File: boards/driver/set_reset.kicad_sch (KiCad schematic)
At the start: 22 parts, among them Q62 MMBT2222, Q63 MMBT2907, Q64 MMBT2222, Q65 MMBT2222

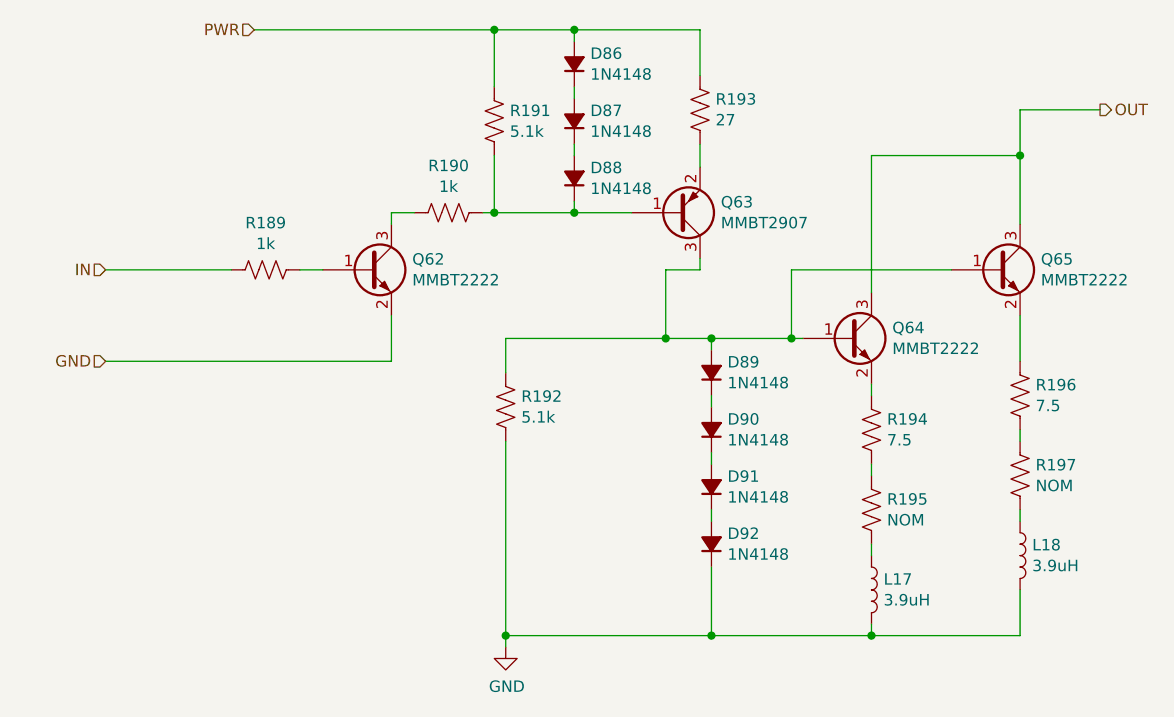
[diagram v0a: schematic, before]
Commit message: Driver: Added a 5V->3.3V LDO to replace the reversed cmod header, added jumpers for the 200R parallel returns, and renamed subcircuit ports to avoid unexpected ground connections.
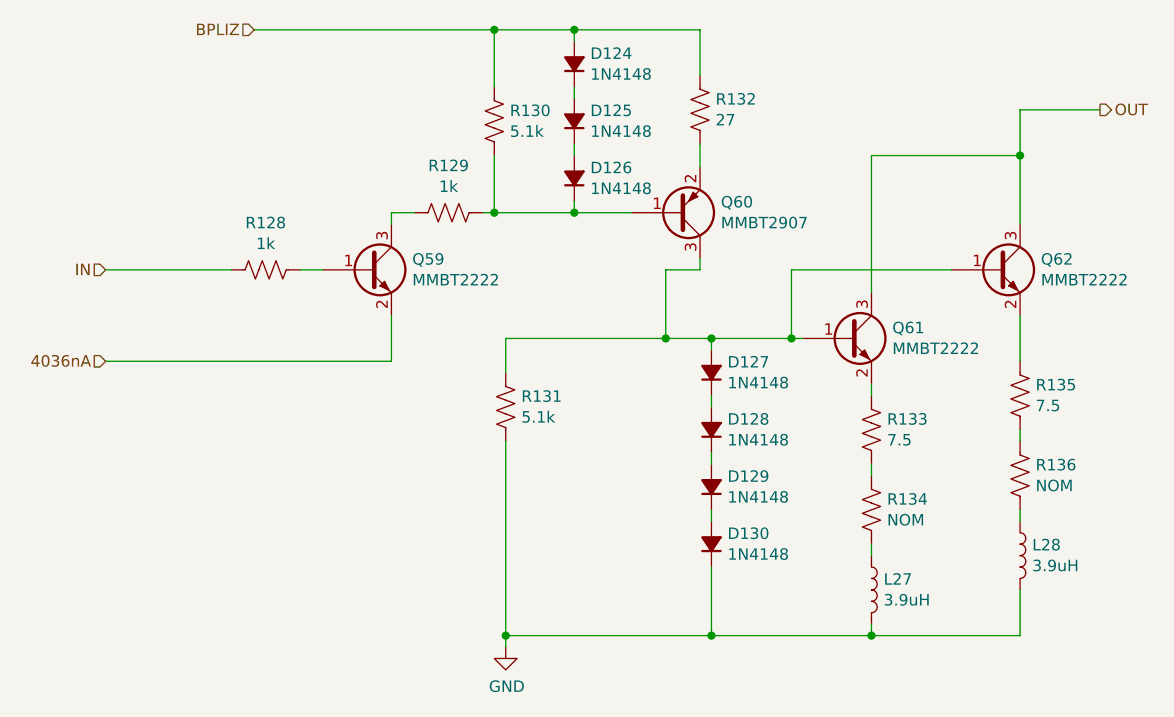
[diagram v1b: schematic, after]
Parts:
- renumbered D86 to D124, D87 to D125, D88 to D126, D89 to D127, D90 to D128, D91 to D129, D92 to D130, L17 to L27, L18 to L28, Q62 to Q59, Q63 to Q60, Q64 to Q61, Q65 to Q62, R189 to R128, R190 to R129, R191 to R130, R192 to R131, R193 to R132, R194 to R133, R195 to R134, R196 to R135, R197 to R136
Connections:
- net GND: no longer Q59.2 (E)
- net PWR renamed BPLIZ
- new net 4036nA: Q59.2 (E)
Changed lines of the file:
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@@
     (stroke (width 0) (type default) (color 0 0 0 0))
   )
-  (hierarchical_label "PWR" (shape input) (at 100.33 63.5 180)
+  (hierarchical_label "BPLIZ" (shape input) (at 100.33 63.5 180)
     (effects (font (size 1.27 1.27)) (justify right))
   )
@@
     (effects (font (size 1.27 1.27)) (justify left))
   )
-  (hierarchical_label "GND" (shape input) (at 83.82 100.33 180)
+  (hierarchical_label "4036nA" (shape input) (at 83.82 100.33 180)
     (effects (font (size 1.27 1.27)) (justify right))
   )
@@
   (symbol (lib_id "Device:R_US") (at 101.6 90.17 270)
     (in_bom yes) (on_board yes)
-    (property "Reference" "R189" (id 0) (at 101.6 84.963 90))
+    (property "Reference" "R128" (id 0) (at 101.6 84.963 90))
     (property "Value" "1k" (id 1) (at 101.6 87.2744 90))
     (property "Footprint" "Resistor_SMD:R_0603_1608Metric" (id 2) (at 101.346 91.186 90)
@@
   (symbol (lib_id "Device:Q_NPN_BEC") (at 113.03 90.17 0)
     (in_bom yes) (on_board yes)
-    (property "Reference" "Q62" (id 0) (at 117.8814 89.0016 0)
+    (property "Reference" "Q59" (id 0) (at 117.8814 89.0016 0)
       (effects (font (size 1.27 1.27)) (justify left))
     )
@@
   (symbol (lib_id "Device:R_US") (at 121.92 83.82 270)
     (in_bom yes) (on_board yes)
-    (property "Reference" "R190" (id 0) (at 121.92 78.613 90))
+    (property "Reference" "R129" (id 0) (at 121.92 78.613 90))
     (property "Value" "1k" (id 1) (at 121.92 80.9244 90))
     (property "Footprint" "Resistor_SMD:R_0603_1608Metric" (id 2) (at 121.666 84.836 90)
@@
   (symbol (lib_id "Device:R_US") (at 127 73.66 0)
     (in_bom yes) (on_board yes)
-    (property "Reference" "R191" (id 0) (at 128.7272 72.4916 0)
+    (property "Reference" "R130" (id 0) (at 128.7272 72.4916 0)
       (effects (font (size 1.27 1.27)) (justify left))
     )
@@
   (symbol (lib_id "Device:D_Small_Filled") (at 135.89 80.01 90)
     (in_bom yes) (on_board yes)
-    (property "Reference" "D88" (id 0) (at 137.668 78.8416 90)
+    (property "Reference" "D126" (id 0) (at 137.668 78.8416 90)
       (effects (font (size 1.27 1.27)) (justify right))
     )
@@
   (symbol (lib_id "Device:D_Small_Filled") (at 135.89 73.66 90)
     (in_bom yes) (on_board yes)
-    (property "Reference" "D87" (id 0) (at 137.668 72.4916 90)
+    (property "Reference" "D125" (id 0) (at 137.668 72.4916 90)
       (effects (font (size 1.27 1.27)) (justify right))
     )
@@
   (symbol (lib_id "Device:D_Small_Filled") (at 135.89 67.31 90)
     (in_bom yes) (on_board yes)
-    (property "Reference" "D86" (id 0) (at 137.668 66.1416 90)
+    (property "Reference" "D124" (id 0) (at 137.668 66.1416 90)
       (effects (font (size 1.27 1.27)) (justify right))
     )
@@
   (symbol (lib_id "Device:Q_PNP_BEC") (at 147.32 83.82 0) (mirror x)
     (in_bom yes) (on_board yes)
-    (property "Reference" "Q63" (id 0) (at 152.1714 82.6516 0)
+    (property "Reference" "Q60" (id 0) (at 152.1714 82.6516 0)
       (effects (font (size 1.27 1.27)) (justify left))
     )
@@
   (symbol (lib_id "Device:R_US") (at 149.86 72.39 0)
     (in_bom yes) (on_board yes)
-    (property "Reference" "R193" (id 0) (at 151.5872 71.2216 0)
+    (property "Reference" "R132" (id 0) (at 151.5872 71.2216 0)
       (effects (font (size 1.27 1.27)) (justify left))
     )
@@
   (symbol (lib_id "Device:D_Small_Filled") (at 151.13 114.3 90)
     (in_bom yes) (on_board yes)
-    (property "Reference" "D91" (id 0) (at 152.908 113.1316 90)
+    (property "Reference" "D129" (id 0) (at 152.908 113.1316 90)
       (effects (font (size 1.27 1.27)) (justify right))
     )
@@
   (symbol (lib_id "Device:D_Small_Filled") (at 151.13 107.95 90)
     (in_bom yes) (on_board yes)
-    (property "Reference" "D90" (id 0) (at 152.908 106.7816 90)
+    (property "Reference" "D128" (id 0) (at 152.908 106.7816 90)
       (effects (font (size 1.27 1.27)) (justify right))
     )
@@
   (symbol (lib_id "Device:D_Small_Filled") (at 151.13 101.6 90)
     (in_bom yes) (on_board yes)
-    (property "Reference" "D89" (id 0) (at 152.908 100.4316 90)
+    (property "Reference" "D127" (id 0) (at 152.908 100.4316 90)
       (effects (font (size 1.27 1.27)) (justify right))
     )
@@
   (symbol (lib_id "Device:D_Small_Filled") (at 151.13 120.65 90)
     (in_bom yes) (on_board yes)
-    (property "Reference" "D92" (id 0) (at 152.908 119.4816 90)
+    (property "Reference" "D130" (id 0) (at 152.908 119.4816 90)
       (effects (font (size 1.27 1.27)) (justify right))
     )
@@
   (symbol (lib_id "Device:R_US") (at 128.27 105.41 0)
     (in_bom yes) (on_board yes)
-    (property "Reference" "R192" (id 0) (at 129.9972 104.2416 0)
+    (property "Reference" "R131" (id 0) (at 129.9972 104.2416 0)
       (effects (font (size 1.27 1.27)) (justify left))
     )
@@
   (symbol (lib_id "power:GND") (at 128.27 132.08 0)
     (in_bom yes) (on_board yes)
-    (property "Reference" "#PWR099" (id 0) (at 128.27 138.43 0)
+    (property "Reference" "#PWR028" (id 0) (at 128.27 138.43 0)
       (effects (font (size 1.27 1.27)) hide)
     )
@@
   (symbol (lib_id "Device:Q_NPN_BEC") (at 166.37 97.79 0)
     (in_bom yes) (on_board yes)
-    (property "Reference" "Q64" (id 0) (at 171.2214 96.6216 0)
+    (property "Reference" "Q61" (id 0) (at 171.2214 96.6216 0)
       (effects (font (size 1.27 1.27)) (justify left))
     )
@@
   (symbol (lib_id "Device:Q_NPN_BEC") (at 182.88 90.17 0)
     (in_bom yes) (on_board yes)
-    (property "Reference" "Q65" (id 0) (at 187.7314 89.0016 0)
+    (property "Reference" "Q62" (id 0) (at 187.7314 89.0016 0)
       (effects (font (size 1.27 1.27)) (justify left))
     )
@@
   (symbol (lib_id "Device:R_US") (at 168.91 107.95 0)
     (in_bom yes) (on_board yes)
-    (property "Reference" "R194" (id 0) (at 170.6372 106.7816 0)
+    (property "Reference" "R133" (id 0) (at 170.6372 106.7816 0)
       (effects (font (size 1.27 1.27)) (justify left))
     )
@@
   (symbol (lib_id "Device:L") (at 168.91 125.73 0)
     (in_bom yes) (on_board yes)
-    (property "Reference" "L17" (id 0) (at 170.2562 124.5616 0)
+    (property "Reference" "L27" (id 0) (at 170.2562 124.5616 0)
       (effects (font (size 1.27 1.27)) (justify left))
     )
@@
   (symbol (lib_id "Device:R_US") (at 185.42 104.14 0)
     (in_bom yes) (on_board yes)
-    (property "Reference" "R196" (id 0) (at 187.1472 102.9716 0)
+    (property "Reference" "R135" (id 0) (at 187.1472 102.9716 0)
       (effects (font (size 1.27 1.27)) (justify left))
     )
@@
   (symbol (lib_id "Device:L") (at 185.42 121.92 0)
     (in_bom yes) (on_board yes)
-    (property "Reference" "L18" (id 0) (at 186.7662 120.7516 0)
+    (property "Reference" "L28" (id 0) (at 186.7662 120.7516 0)
       (effects (font (size 1.27 1.27)) (justify left))
     )
@@
   (symbol (lib_id "Device:R_US") (at 168.91 116.84 0)
     (in_bom yes) (on_board yes)
-    (property "Reference" "R195" (id 0) (at 170.6372 115.6716 0)
+    (property "Reference" "R134" (id 0) (at 170.6372 115.6716 0)
       (effects (font (size 1.27 1.27)) (justify left))
     )
@@
   (symbol (lib_id "Device:R_US") (at 185.42 113.03 0)
     (in_bom yes) (on_board yes)
-    (property "Reference" "R197" (id 0) (at 187.1472 111.8616 0)
-      (effects (font (size 1.27 1.27)) (justify left))
-    )
+    (property "Reference" "R136" (id 0) (at 187.1472 111.8616 0)
+      (effects (font (size 1.27 1.27)) (justify left))
+    )

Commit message: Driver: incorporated most changes from the test board, and began layout
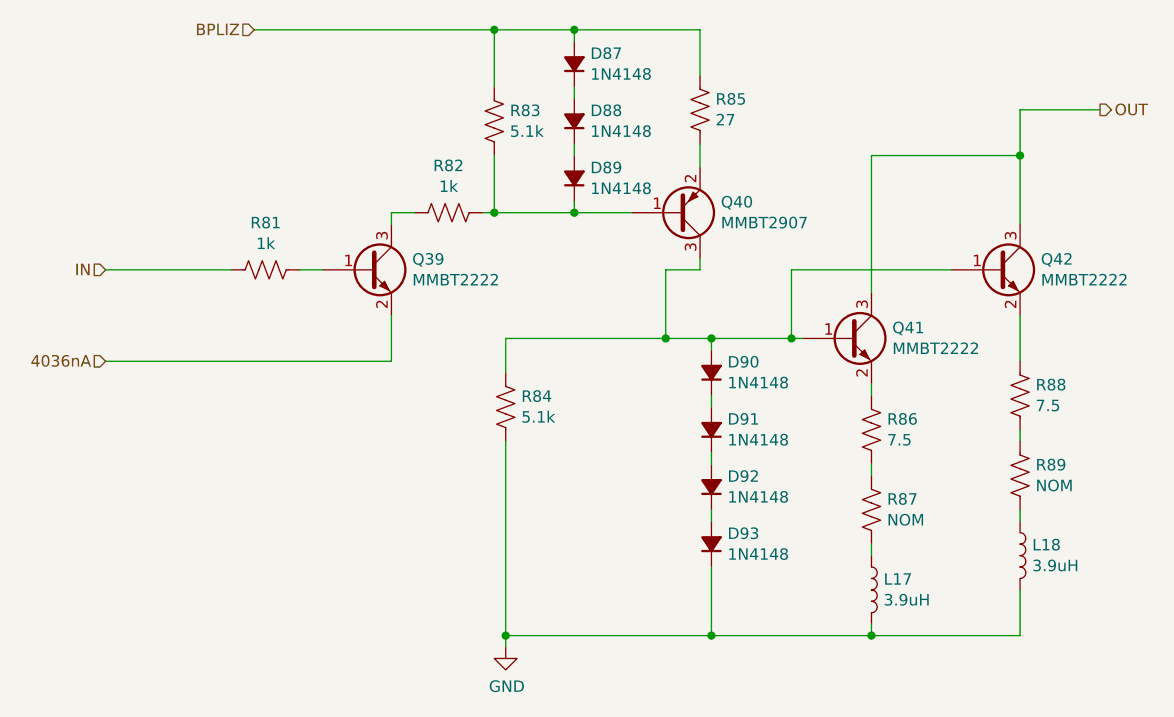
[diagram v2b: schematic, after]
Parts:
- D87: renamed from D124; footprint Diode_SMD:D_SOD-323 -> lachesis:D_SOD-323
- D88: renamed from D125; footprint Diode_SMD:D_SOD-323 -> lachesis:D_SOD-323
- D89: renamed from D126; footprint Diode_SMD:D_SOD-323 -> lachesis:D_SOD-323
- D90: renamed from D127; footprint Diode_SMD:D_SOD-323 -> lachesis:D_SOD-323
- D91: renamed from D128; footprint Diode_SMD:D_SOD-323 -> lachesis:D_SOD-323
- D92: renamed from D129; footprint Diode_SMD:D_SOD-323 -> lachesis:D_SOD-323
- D93: renamed from D130; footprint Diode_SMD:D_SOD-323 -> lachesis:D_SOD-323
- L17: renamed from L27; footprint Inductor_SMD:L_1812_4532Metric -> lachesis:API_Delevan_1812R
- L18: renamed from L28; footprint Inductor_SMD:L_1812_4532Metric -> lachesis:API_Delevan_1812R
- renumbered Q59 to Q39, Q60 to Q40, Q61 to Q41, Q62 to Q42, R128 to R81, R129 to R82, R130 to R83, R131 to R84, R132 to R85, R133 to R86, R134 to R87, R135 to R88, R136 to R89

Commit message: Driver: minor schematic cleanup and populated all of the BOM except for resistors
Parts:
- D87, D88, D89, D90, D91, D92, D93: MPN (none) -> 1N4148WS; Manufacturer (none) -> SMC Diode Solutions; Package (none) -> SOD-323; Rating (none) -> 300mA
- L17, L18: MPN (none) -> 1812R-392J; Manufacturer (none) -> API Delevan Inc; Package (none) -> 1812
- Q39, Q41, Q42: MPN (none) -> MMBT2222ALT1HTSA1; Manufacturer (none) -> Infineon Technologies; Package (none) -> SOT-23-3
- Q40: MPN (none) -> MMBT2907ALT1HTSA1; Manufacturer (none) -> Infineon Technologies; Package (none) -> SOT-23-3
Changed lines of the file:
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@@
+      (effects (font (size 1.27 1.27)) hide)
+    )
+    (property "MPN" "MMBT2222ALT1HTSA1" (id 6) (at 113.03 90.17 0)
+      (effects (font (size 1.27 1.27)) hide)
+    )
+    (property "Manufacturer" "Infineon Technologies" (id 7) (at 113.03 90.17 0)
+      (effects (font (size 1.27 1.27)) hide)
+    )
+    (property "Description" "TRANS NPN 40V 0.6A SOT-23" (id 8) (at 113.03 90.17 0)
+      (effects (font (size 1.27 1.27)) hide)
+    )
+    (property "Package" "SOT-23-3" (id 9) (at 113.03 90.17 0)
       (effects (font (size 1.27 1.27)) hide)
     )
@@
       (effects (font (size 1.27 1.27)) hide)
     )
+    (property "MPN" "1N4148WS" (id 6) (at 135.89 80.01 0)
+      (effects (font (size 1.27 1.27)) hide)
+    )
+    (property "Manufacturer" "SMC Diode Solutions" (id 7) (at 135.89 80.01 0)
+      (effects (font (size 1.27 1.27)) hide)
+    )
+    (property "Description" "DIODE GEN PURP 75V 300MA SOD323" (id 8) (at 135.89 80.01 0)
+      (effects (font (size 1.27 1.27)) hide)
+    )
+    (property "Package" "SOD-323" (id 9) (at 135.89 80.01 0)
+      (effects (font (size 1.27 1.27)) hide)
+    )
+    (property "Rating" "300mA" (id 10) (at 135.89 80.01 0)
+      (effects (font (size 1.27 1.27)) hide)
+    )
     (pin "1")
     (pin "2")
@@
       (effects (font (size 1.27 1.27)) hide)
     )
+    (property "MPN" "1N4148WS" (id 6) (at 135.89 73.66 0)
+      (effects (font (size 1.27 1.27)) hide)
+    )
+    (property "Manufacturer" "SMC Diode Solutions" (id 7) (at 135.89 73.66 0)
+      (effects (font (size 1.27 1.27)) hide)
+    )
+    (property "Description" "DIODE GEN PURP 75V 300MA SOD323" (id 8) (at 135.89 73.66 0)
+      (effects (font (size 1.27 1.27)) hide)
+    )
+    (property "Package" "SOD-323" (id 9) (at 135.89 73.66 0)
+      (effects (font (size 1.27 1.27)) hide)
+    )
+    (property "Rating" "300mA" (id 10) (at 135.89 73.66 0)
+      (effects (font (size 1.27 1.27)) hide)
+    )
     (pin "1")
     (pin "2")
@@
       (effects (font (size 1.27 1.27)) hide)
     )
+    (property "MPN" "1N4148WS" (id 6) (at 135.89 67.31 0)
+      (effects (font (size 1.27 1.27)) hide)
+    )
+    (property "Manufacturer" "SMC Diode Solutions" (id 7) (at 135.89 67.31 0)
+      (effects (font (size 1.27 1.27)) hide)
+    )
+    (property "Description" "DIODE GEN PURP 75V 300MA SOD323" (id 8) (at 135.89 67.31 0)
+      (effects (font (size 1.27 1.27)) hide)
+    )
+    (property "Package" "SOD-323" (id 9) (at 135.89 67.31 0)
+      (effects (font (size 1.27 1.27)) hide)
+    )
+    (property "Rating" "300mA" (id 10) (at 135.89 67.31 0)
+      (effects (font (size 1.27 1.27)) hide)
+    )
     (pin "1")
     (pin "2")
@@
       (effects (font (size 1.27 1.27)) hide)
     )
+    (property "MPN" "MMBT2907ALT1HTSA1" (id 6) (at 147.32 83.82 0)
+      (effects (font (size 1.27 1.27)) hide)
+    )
+    (property "Manufacturer" "Infineon Technologies" (id 7) (at 147.32 83.82 0)
+      (effects (font (size 1.27 1.27)) hide)
+    )
+    (property "Description" "TRANS PNP 60V 0.6A SOT23" (id 8) (at 147.32 83.82 0)
+      (effects (font (size 1.27 1.27)) hide)
+    )
+    (property "Package" "SOT-23-3" (id 9) (at 147.32 83.82 0)
+      (effects (font (size 1.27 1.27)) hide)
+    )
     (pin "1")
     (pin "2")
@@
       (effects (font (size 1.27 1.27)) hide)
     )
+    (property "MPN" "1N4148WS" (id 6) (at 151.13 114.3 0)
+      (effects (font (size 1.27 1.27)) hide)
+    )
+    (property "Manufacturer" "SMC Diode Solutions" (id 7) (at 151.13 114.3 0)
+      (effects (font (size 1.27 1.27)) hide)
+    )
+    (property "Description" "DIODE GEN PURP 75V 300MA SOD323" (id 8) (at 151.13 114.3 0)
+      (effects (font (size 1.27 1.27)) hide)
+    )
+    (property "Package" "SOD-323" (id 9) (at 151.13 114.3 0)
+      (effects (font (size 1.27 1.27)) hide)
+    )
+    (property "Rating" "300mA" (id 10) (at 151.13 114.3 0)
+      (effects (font (size 1.27 1.27)) hide)
+    )
     (pin "1")
     (pin "2")
@@
       (effects (font (size 1.27 1.27)) hide)
     )
+    (property "MPN" "1N4148WS" (id 6) (at 151.13 107.95 0)
+      (effects (font (size 1.27 1.27)) hide)
+    )
+    (property "Manufacturer" "SMC Diode Solutions" (id 7) (at 151.13 107.95 0)
+      (effects (font (size 1.27 1.27)) hide)
+    )
+    (property "Description" "DIODE GEN PURP 75V 300MA SOD323" (id 8) (at 151.13 107.95 0)
+      (effects (font (size 1.27 1.27)) hide)
+    )
+    (property "Package" "SOD-323" (id 9) (at 151.13 107.95 0)
+      (effects (font (size 1.27 1.27)) hide)
+    )
+    (property "Rating" "300mA" (id 10) (at 151.13 107.95 0)
+      (effects (font (size 1.27 1.27)) hide)
+    )
     (pin "1")
     (pin "2")
@@
       (effects (font (size 1.27 1.27)) hide)
     )
+    (property "MPN" "1N4148WS" (id 6) (at 151.13 101.6 0)
+      (effects (font (size 1.27 1.27)) hide)
+    )
+    (property "Manufacturer" "SMC Diode Solutions" (id 7) (at 151.13 101.6 0)
+      (effects (font (size 1.27 1.27)) hide)
+    )
+    (property "Description" "DIODE GEN PURP 75V 300MA SOD323" (id 8) (at 151.13 101.6 0)
+      (effects (font (size 1.27 1.27)) hide)
+    )
+    (property "Package" "SOD-323" (id 9) (at 151.13 101.6 0)
+      (effects (font (size 1.27 1.27)) hide)
+    )
+    (property "Rating" "300mA" (id 10) (at 151.13 101.6 0)
+      (effects (font (size 1.27 1.27)) hide)
+    )
     (pin "1")
     (pin "2")
@@
     )
     (property "Digikey" "https://www.digikey.com/en/products/detail/smc-diode-solutions/1N4148WSTR/6022449" (id 5) (at 191.77 147.32 90)
+      (effects (font (size 1.27 1.27)) hide)
+    )
+    (property "MPN" "1N4148WS" (id 6) (at 151.13 120.65 0)
+      (effects (font (size 1.27 1.27)) hide)
+    )
+    (property "Manufacturer" "SMC Diode Solutions" (id 7) (at 151.13 120.65 0)
+      (effects (font (size 1.27 1.27)) hide)
+    )
+    (property "Description" "DIODE GEN PURP 75V 300MA SOD323" (id 8) (at 151.13 120.65 0)
+      (effects (font (size 1.27 1.27)) hide)
+    )
+    (property "Package" "SOD-323" (id 9) (at 151.13 120.65 0)
+      (effects (font (size 1.27 1.27)) hide)
+    )
+    (property "Rating" "300mA" (id 10) (at 151.13 120.65 0)
       (effects (font (size 1.27 1.27)) hide)
     )
@@
       (effects (font (size 1.27 1.27)) hide)
     )
+    (property "MPN" "MMBT2222ALT1HTSA1" (id 6) (at 166.37 97.79 0)
+      (effects (font (size 1.27 1.27)) hide)
+    )
+    (property "Manufacturer" "Infineon Technologies" (id 7) (at 166.37 97.79 0)
+      (effects (font (size 1.27 1.27)) hide)
+    )
+    (property "Description" "TRANS NPN 40V 0.6A SOT-23" (id 8) (at 166.37 97.79 0)
+      (effects (font (size 1.27 1.27)) hide)
+    )
+    (property "Package" "SOT-23-3" (id 9) (at 166.37 97.79 0)
+      (effects (font (size 1.27 1.27)) hide)
+    )
     (pin "1")
     (pin "2")
@@
       (effects (font (size 1.27 1.27)) hide)
     )
+    (property "MPN" "MMBT2222ALT1HTSA1" (id 6) (at 182.88 90.17 0)
+      (effects (font (size 1.27 1.27)) hide)
+    )
+    (property "Manufacturer" "Infineon Technologies" (id 7) (at 182.88 90.17 0)
+      (effects (font (size 1.27 1.27)) hide)
+    )
+    (property "Description" "TRANS NPN 40V 0.6A SOT-23" (id 8) (at 182.88 90.17 0)
+      (effects (font (size 1.27 1.27)) hide)
+    )
+    (property "Package" "SOT-23-3" (id 9) (at 182.88 90.17 0)
+      (effects (font (size 1.27 1.27)) hide)
+    )
     (pin "1")
     (pin "2")
@@
       (effects (font (size 1.27 1.27)) hide)
     )
+    (property "MPN" "1812R-392J" (id 9) (at 168.91 125.73 0)
+      (effects (font (size 1.27 1.27)) hide)
+    )
+    (property "Manufacturer" "API Delevan Inc" (id 10) (at 168.91 125.73 0)
+      (effects (font (size 1.27 1.27)) hide)
+    )
+    (property "Description" "FIXED IND 3.9UH 472MA 900MOHM SM" (id 11) (at 168.91 125.73 0)
+      (effects (font (size 1.27 1.27)) hide)
+    )
+    (property "Package" "1812" (id 12) (at 168.91 125.73 0)
+      (effects (font (size 1.27 1.27)) hide)
+    )
     (pin "1")
     (pin "2")
@@
       (effects (font (size 1.27 1.27)) hide)
     )
+    (property "MPN" "1812R-392J" (id 9) (at 185.42 121.92 0)
+      (effects (font (size 1.27 1.27)) hide)
+    )
+    (property "Manufacturer" "API Delevan Inc" (id 10) (at 185.42 121.92 0)
+      (effects (font (size 1.27 1.27)) hide)
+    )
+    (property "Description" "FIXED IND 3.9UH 472MA 900MOHM SM" (id 11) (at 185.42 121.92 0)
+      (effects (font (size 1.27 1.27)) hide)
+    )
+    (property "Package" "1812" (id 12) (at 185.42 121.92 0)
+      (effects (font (size 1.27 1.27)) hide)
+    )
